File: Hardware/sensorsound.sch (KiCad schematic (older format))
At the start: 20 parts, among them U7 LM324

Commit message: BOM file .csv
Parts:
- D4, D5: value RB751V40T1_1 -> RB751S40T1G; footprint (none) -> Diode_SMD:D_SOD-123; manf# (none) -> NRVB120VLSFT1G
- MK1: manf# 25R4387 -> POM-3044P-R
- RV1: footprint Potentiometer_THT:Potentiometer_Bourns_3296W_Vertical -> Potentiometer_THT:Potentiometer_Bourns_3386P_Vertical; manf# (none) -> 3362P-1-104LF
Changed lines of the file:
@@
 F 1 "Microphone" V 2330 3795 50  0000 L CNN
 F 2 "TerminalBlock_TE-Connectivity:TerminalBlock_TE_282834-2_1x02_P2.54mm_Horizontal" V 2590 4020 50  0001 C CNN
-F 3 "http://www.farnell.com/datasheets/1660938.pdf" V 2590 4020 50  0001 C CNN
-F 4 "25R4387" H 0   0   50  0001 C CNN "manf#"
+F 3 "https://www.mouser.mx/datasheet/2/334/POM-3044P-R-60075.pdf" V 2590 4020 50  0001 C CNN
+F 4 "POM-3044P-R" H 0   0   50  0001 C CNN "manf#"
 	1    2590 3920
 	1    0    0    -1
@@
 F 0 "RV1" V 4910 2850 50  0000 C CNN
 F 1 "100K GAIN" V 4620 2770 50  0000 C CNN
-F 2 "Potentiometer_THT:Potentiometer_Bourns_3296W_Vertical" H 4710 2770 50  0001 C CNN
-F 3 "~" H 4710 2770 50  0001 C CNN
+F 2 "Potentiometer_THT:Potentiometer_Bourns_3386P_Vertical" H 4710 2770 50  0001 C CNN
+F 3 "https://www.mouser.mx/datasheet/2/54/362-776956.pdf" H 4710 2770 50  0001 C CNN
+F 4 "3362P-1-104LF" H 0   0   50  0001 C CNN "manf#"
 	1    4710 2770
 	0    -1   -1   0
@@
 P 6570 3410
 F 0 "D4" H 6570 3320 50  0000 C CNN
-F 1 "RB751V40T1_1" H 6570 3510 50  0000 C CNN
-F 2 "" V 6570 3410 50  0001 C CNN
-F 3 "~" V 6570 3410 50  0001 C CNN
+F 1 "RB751S40T1G" H 6570 3510 50  0000 C CNN
+F 2 "Diode_SMD:D_SOD-123" V 6570 3410 50  0001 C CNN
+F 3 "https://www.mouser.mx/datasheet/2/308/MBR120VLSFT1-D-1074021.pdf" V 6570 3410 50  0001 C CNN
+F 4 "NRVB120VLSFT1G" H 0   0   50  0001 C CNN "manf#"
 	1    6570 3410
 	-1   0    0    1
@@
 P 7060 3920
 F 0 "D5" H 7060 3810 50  0000 C CNN
-F 1 "RB751V40T1_1" H 7060 4040 50  0000 C CNN
-F 2 "" V 7060 3920 50  0001 C CNN
-F 3 "~" V 7060 3920 50  0001 C CNN
+F 1 "RB751S40T1G" H 7060 4040 50  0000 C CNN
+F 2 "Diode_SMD:D_SOD-123" V 7060 3920 50  0001 C CNN
+F 3 "https://www.mouser.mx/datasheet/2/308/MBR120VLSFT1-D-1074021.pdf" V 7060 3920 50  0001 C CNN
+F 4 "NRVB120VLSFT1G" H 0   0   50  0001 C CNN "manf#"
 	1    7060 3920
 	-1   0    0    1

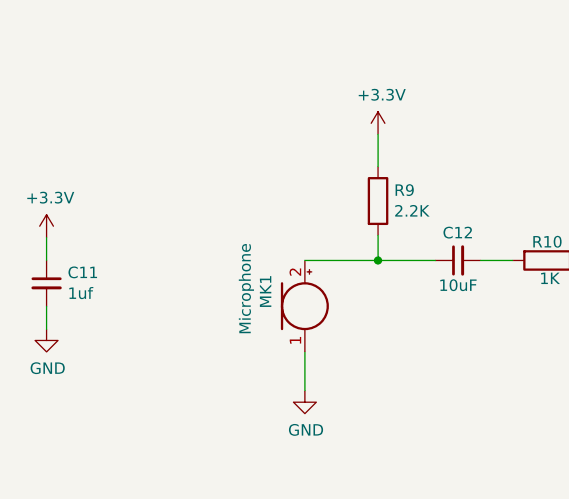
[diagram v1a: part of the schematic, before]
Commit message: add cap amp voltage
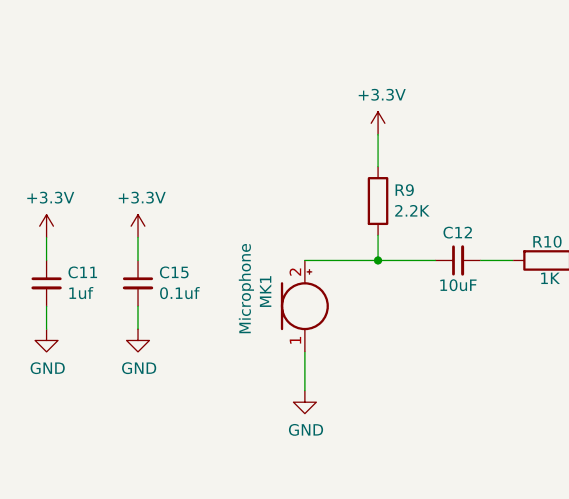
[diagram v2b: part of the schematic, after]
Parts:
- added C15: 0.1uf, symbol Device:C_Small
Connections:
- net +3V3: now also C15.1
- net GND: now also C15.2
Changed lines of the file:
@@
 	1    0    0    -1
 $EndComp
+$Comp
+L Device:C_Small C15
+U 1 1 5C5DECA3
+P 1860 3820
+F 0 "C15" H 1952 3866 50  0000 L CNN
+F 1 "0.1uf" H 1952 3775 50  0000 L CNN
+F 2 "" H 1860 3820 50  0001 C CNN
+F 3 "~" H 1860 3820 50  0001 C CNN
+	1    1860 3820
+	1    0    0    -1
+$EndComp
+$Comp
+L power:GND #PWR02
+U 1 1 5C5DEDF4
+P 1860 4020
+F 0 "#PWR02" H 1860 3770 50  0001 C CNN
+F 1 "GND" H 1865 3847 50  0000 C CNN
+F 2 "" H 1860 4020 50  0001 C CNN
+F 3 "" H 1860 4020 50  0001 C CNN
+	1    1860 4020
+	1    0    0    -1
+$EndComp
+$Comp
+L power:+3.3V #PWR01
+U 1 1 5C5DEED5
+P 1860 3620
+F 0 "#PWR01" H 1860 3470 50  0001 C CNN
+F 1 "+3.3V" H 1875 3793 50  0000 C CNN
+F 2 "" H 1860 3620 50  0001 C CNN
+F 3 "" H 1860 3620 50  0001 C CNN
+	1    1860 3620
+	1    0    0    -1
+$EndComp
+Wire Wire Line
+	1860 3620 1860 3720
+Wire Wire Line
+	1860 3920 1860 4020
 $EndSCHEMATC

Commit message: footprint c15
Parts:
- C15: footprint (none) -> Capacitor_SMD:C_0805_2012Metric_Pad1.15x1.40mm_HandSolder; manf# (none) -> 08056C104JAZ2A
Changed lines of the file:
@@
 F 0 "C15" H 1952 3866 50  0000 L CNN
 F 1 "0.1uf" H 1952 3775 50  0000 L CNN
-F 2 "" H 1860 3820 50  0001 C CNN
-F 3 "~" H 1860 3820 50  0001 C CNN
+F 2 "Capacitor_SMD:C_0805_2012Metric_Pad1.15x1.40mm_HandSolder" H 1860 3820 50  0001 C CNN
+F 3 "https://www.mouser.mx/datasheet/2/40/X7RDielectric-777024.pdf" H 1860 3820 50  0001 C CNN
+F 4 "08056C104JAZ2A" H 0   0   50  0001 C CNN "manf#"
 	1    1860 3820
 	1    0    0    -1
